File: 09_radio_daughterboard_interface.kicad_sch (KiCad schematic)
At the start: 60 parts, among them J2300 DF40C 60-pin optional radio d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, Q2300 2N7002K radio-PG USB enable, U2300 TPS259470ARPW 2A reverse-bloc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, U2301 TLV803EA43 4.3V radio rail su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, U2302 SN74LVC1G17DBVR radio PG leve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, U2303 TS3USB30E default-disconnecte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, U2304 TPS2553D radio codec VBUS gat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, U2305 USBLC6-2P6 radio codec USB ESD

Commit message: Stamp generation-time BOM catalog; close 378 procurement gaps
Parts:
- C2300: MPN (none) -> GRM155R71H472KA01; Manufacturer (none) -> Murata
- C2301, C2308: MPN (none) -> GRM31CR71E106KA12L; Manufacturer (none) -> Murata
- C2302, C2304, C2305, C2306: MPN (none) -> GRM188R71H104KA93D; Manufacturer (none) -> Murata
- C2303: MPN (none) -> GRM31CZ71C226ME15L; Manufacturer (none) -> Murata
- C2307: MPN (none) -> GRM21BR71E105KA12L; Manufacturer (none) -> Murata
- R2300, R2307: MPN (none) -> RC0603FR-07100KL; Manufacturer (none) -> Yageo
- R2301: MPN (none) -> RT0603BRD071K65L; Manufacturer (none) -> Yageo
- R2302: MPN (none) -> RC0603FR-072K2L; Manufacturer (none) -> Yageo
- R2303, R2305, R2306: MPN (none) -> RC0603FR-0710KL; Manufacturer (none) -> Yageo
- R2304: MPN (none) -> RC0603FR-0720KL; Manufacturer (none) -> Yageo
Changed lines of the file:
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@@
   (property "Footprint" "Resistor_SMD:R_0603_1608Metric" (at 20.32 76.2 0) (effects (font (size 1.27 1.27)) (hide yes)))
   (property "Datasheet" "" (at 20.32 76.2 0) (effects (font (size 1.27 1.27)) (hide yes)))
+  (property "Manufacturer" "Yageo" (at 20.32 76.2 0) (effects (font (size 1.27 1.27)) (hide yes)))
+  (property "MPN" "RC0603FR-07100KL" (at 20.32 76.2 0) (effects (font (size 1.27 1.27)) (hide yes)))
   (pin "1")
   (pin "2")
@@
   (property "Footprint" "Resistor_SMD:R_0603_1608Metric" (at 20.32 88.9 0) (effects (font (size 1.27 1.27)) (hide yes)))
   (property "Datasheet" "" (at 20.32 88.9 0) (effects (font (size 1.27 1.27)) (hide yes)))
+  (property "Manufacturer" "Yageo" (at 20.32 88.9 0) (effects (font (size 1.27 1.27)) (hide yes)))
+  (property "MPN" "RT0603BRD071K65L" (at 20.32 88.9 0) (effects (font (size 1.27 1.27)) (hide yes)))
   (pin "1")
   (pin "2")
@@
   (property "Footprint" "Capacitor_SMD:C_0402_1005Metric" (at 20.32 101.6 0) (effects (font (size 1.27 1.27)) (hide yes)))
   (property "Datasheet" "" (at 20.32 101.6 0) (effects (font (size 1.27 1.27)) (hide yes)))
+  (property "Manufacturer" "Murata" (at 20.32 101.6 0) (effects (font (size 1.27 1.27)) (hide yes)))
+  (property "MPN" "GRM155R71H472KA01" (at 20.32 101.6 0) (effects (font (size 1.27 1.27)) (hide yes)))
   (pin "1")
   (pin "2")
@@
   (property "Footprint" "Capacitor_SMD:C_1206_3216Metric" (at 20.32 114.3 0) (effects (font (size 1.27 1.27)) (hide yes)))
   (property "Datasheet" "" (at 20.32 114.3 0) (effects (font (size 1.27 1.27)) (hide yes)))
+  (property "Manufacturer" "Murata" (at 20.32 114.3 0) (effects (font (size 1.27 1.27)) (hide yes)))
+  (property "MPN" "GRM31CR71E106KA12L" (at 20.32 114.3 0) (effects (font (size 1.27 1.27)) (hide yes)))
   (pin "1")
   (pin "2")
@@
   (property "Footprint" "Capacitor_SMD:C_0603_1608Metric" (at 20.32 127 0) (effects (font (size 1.27 1.27)) (hide yes)))
   (property "Datasheet" "" (at 20.32 127 0) (effects (font (size 1.27 1.27)) (hide yes)))
+  (property "Manufacturer" "Murata" (at 20.32 127 0) (effects (font (size 1.27 1.27)) (hide yes)))
+  (property "MPN" "GRM188R71H104KA93D" (at 20.32 127 0) (effects (font (size 1.27 1.27)) (hide yes)))
   (pin "1")
   (pin "2")
@@
   (property "Footprint" "Capacitor_SMD:C_1206_3216Metric" (at 20.32 139.7 0) (effects (font (size 1.27 1.27)) (hide yes)))
   (property "Datasheet" "" (at 20.32 139.7 0) (effects (font (size 1.27 1.27)) (hide yes)))
+  (property "Manufacturer" "Murata" (at 20.32 139.7 0) (effects (font (size 1.27 1.27)) (hide yes)))
+  (property "MPN" "GRM31CZ71C226ME15L" (at 20.32 139.7 0) (effects (font (size 1.27 1.27)) (hide yes)))
   (pin "1")
   (pin "2")
@@
   (property "Footprint" "Capacitor_SMD:C_0603_1608Metric" (at 20.32 152.4 0) (effects (font (size 1.27 1.27)) (hide yes)))
   (property "Datasheet" "" (at 20.32 152.4 0) (effects (font (size 1.27 1.27)) (hide yes)))
+  (property "Manufacturer" "Murata" (at 20.32 152.4 0) (effects (font (size 1.27 1.27)) (hide yes)))
+  (property "MPN" "GRM188R71H104KA93D" (at 20.32 152.4 0) (effects (font (size 1.27 1.27)) (hide yes)))
   (pin "1")
   (pin "2")
@@
   (property "Footprint" "Resistor_SMD:R_0603_1608Metric" (at 224.79 115.57 0) (effects (font (size 1.27 1.27)) (hide yes)))
   (property "Datasheet" "" (at 224.79 115.57 0) (effects (font (size 1.27 1.27)) (hide yes)))
+  (property "Manufacturer" "Yageo" (at 224.79 115.57 0) (effects (font (size 1.27 1.27)) (hide yes)))
+  (property "MPN" "RC0603FR-072K2L" (at 224.79 115.57 0) (effects (font (size 1.27 1.27)) (hide yes)))
   (pin "1")
   (pin "2")
@@
   (property "Footprint" "Resistor_SMD:R_0603_1608Metric" (at 260.35 115.57 0) (effects (font (size 1.27 1.27)) (hide yes)))
   (property "Datasheet" "" (at 260.35 115.57 0) (effects (font (size 1.27 1.27)) (hide yes)))
+  (property "Manufacturer" "Yageo" (at 260.35 115.57 0) (effects (font (size 1.27 1.27)) (hide yes)))
+  (property "MPN" "RC0603FR-0710KL" (at 260.35 115.57 0) (effects (font (size 1.27 1.27)) (hide yes)))
   (pin "1")
   (pin "2")
@@
   (property "Footprint" "Resistor_SMD:R_0603_1608Metric" (at 299.72 115.57 0) (effects (font (size 1.27 1.27)) (hide yes)))
   (property "Datasheet" "" (at 299.72 115.57 0) (effects (font (size 1.27 1.27)) (hide yes)))
+  (property "Manufacturer" "Yageo" (at 299.72 115.57 0) (effects (font (size 1.27 1.27)) (hide yes)))
+  (property "MPN" "RC0603FR-0720KL" (at 299.72 115.57 0) (effects (font (size 1.27 1.27)) (hide yes)))
   (pin "1")
   (pin "2")
@@
   (property "Footprint" "Capacitor_SMD:C_0603_1608Metric" (at 350.52 124.46 0) (effects (font (size 1.27 1.27)) (hide yes)))
   (property "Datasheet" "" (at 350.52 124.46 0) (effects (font (size 1.27 1.27)) (hide yes)))
+  (property "Manufacturer" "Murata" (at 350.52 124.46 0) (effects (font (size 1.27 1.27)) (hide yes)))
+  (property "MPN" "GRM188R71H104KA93D" (at 350.52 124.46 0) (effects (font (size 1.27 1.27)) (hide yes)))
   (pin "1")
   (pin "2")
@@
   (property "Footprint" "Resistor_SMD:R_0603_1608Metric" (at 420.37 76.2 0) (effects (font (size 1.27 1.27)) (hide yes)))
   (property "Datasheet" "" (at 420.37 76.2 0) (effects (font (size 1.27 1.27)) (hide yes)))
+  (property "Manufacturer" "Yageo" (at 420.37 76.2 0) (effects (font (size 1.27 1.27)) (hide yes)))
+  (property "MPN" "RC0603FR-0710KL" (at 420.37 76.2 0) (effects (font (size 1.27 1.27)) (hide yes)))
   (pin "1")
   (pin "2")
@@
   (property "Footprint" "Resistor_SMD:R_0603_1608Metric" (at 420.37 88.9 0) (effects (font (size 1.27 1.27)) (hide yes)))
   (property "Datasheet" "" (at 420.37 88.9 0) (effects (font (size 1.27 1.27)) (hide yes)))
+  (property "Manufacturer" "Yageo" (at 420.37 88.9 0) (effects (font (size 1.27 1.27)) (hide yes)))
+  (property "MPN" "RC0603FR-0710KL" (at 420.37 88.9 0) (effects (font (size 1.27 1.27)) (hide yes)))
   (pin "1")
   (pin "2")
@@
   (property "Footprint" "Resistor_SMD:R_0603_1608Metric" (at 20.32 228.6 0) (effects (font (size 1.27 1.27)) (hide yes)))
   (property "Datasheet" "" (at 20.32 228.6 0) (effects (font (size 1.27 1.27)) (hide yes)))
+  (property "Manufacturer" "Yageo" (at 20.32 228.6 0) (effects (font (size 1.27 1.27)) (hide yes)))
+  (property "MPN" "RC0603FR-07100KL" (at 20.32 228.6 0) (effects (font (size 1.27 1.27)) (hide yes)))
   (pin "1")
   (pin "2")
@@
   (property "Footprint" "Capacitor_SMD:C_0603_1608Metric" (at 20.32 254 0) (effects (font (size 1.27 1.27)) (hide yes)))
   (property "Datasheet" "" (at 20.32 254 0) (effects (font (size 1.27 1.27)) (hide yes)))
+  (property "Manufacturer" "Murata" (at 20.32 254 0) (effects (font (size 1.27 1.27)) (hide yes)))
+  (property "MPN" "GRM188R71H104KA93D" (at 20.32 254 0) (effects (font (size 1.27 1.27)) (hide yes)))
   (pin "1")
   (pin "2")
@@
   (property "Footprint" "Capacitor_SMD:C_0805_2012Metric" (at 430.53 241.3 0) (effects (font (size 1.27 1.27)) (hide yes)))
   (property "Datasheet" "" (at 430.53 241.3 0) (effects (font (size 1.27 1.27)) (hide yes)))
+  (property "Manufacturer" "Murata" (at 430.53 241.3 0) (effects (font (size 1.27 1.27)) (hide yes)))
+  (property "MPN" "GRM21BR71E105KA12L" (at 430.53 241.3 0) (effects (font (size 1.27 1.27)) (hide yes)))
   (pin "1")
   (pin "2")
@@
   (property "Footprint" "Capacitor_SMD:C_1206_3216Metric" (at 430.53 254 0) (effects (font (size 1.27 1.27)) (hide yes)))
   (property "Datasheet" "" (at 430.53 254 0) (effects (font (size 1.27 1.27)) (hide yes)))
-  (pin "1")
-  (pin "2")
+  (property "Manufacturer" "Murata" (at 430.53 254 0) (effects (font (size 1.27 1.27)) (hide yes)))
+  (property "MPN" "GRM31CR71E106KA12L" (at 430.53 254 0) (effects (font (size 1.27 1.27)) (hide yes)))
+  (pin "1")
+  (pin "2")

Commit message: Swap radio daughterboard connector: DF40-60 -> FH12-30S FFC
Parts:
- J2300: value DF40C 60-pin optional radio daughterboard plug -> FH12-30S 30-pin radio daughterboard FFC; footprint Connector_Hirose_DF40:Hirose_DF40C-60DP-0.4V_2x30-1MP_P0.4mm -> Connector_FFC-FPC:Hirose_FH12-30S-0.5SH_1x30-1MP_P0.50mm_Horizontal; symbol Conn_02x30_MP:Conn_02x30_MP -> Conn_01x30_FFC_MP:Conn_01x30_FFC_MP
- R2340: value 4.7k J2300 pin 23 signal isolation -> 4.7k J2300 pin 11 signal isolation
- R2341: value 4.7k J2300 pin 24 signal isolation -> 4.7k J2300 pin 12 signal isolation
- R2342: value 4.7k J2300 pin 25 signal isolation -> 4.7k J2300 pin 13 signal isolation
- R2343: value 4.7k J2300 pin 26 signal isolation -> 4.7k J2300 pin 14 signal isolation
- R2344: value 4.7k J2300 pin 28 signal isolation -> 4.7k J2300 pin 15 signal isolation
- R2345: value 4.7k J2300 pin 29 signal isolation -> 4.7k J2300 pin 16 signal isolation
- R2346: value 4.7k J2300 pin 30 signal isolation -> 4.7k J2300 pin 17 signal isolation
- R2347: value 4.7k J2300 pin 31 signal isolation -> 4.7k J2300 pin 18 signal isolation
- R2348: value 4.7k J2300 pin 33 signal isolation -> 4.7k J2300 pin 20 signal isolation
- R2349: value 4.7k J2300 pin 34 signal isolation -> 4.7k J2300 pin 21 signal isolation
- R2350: value 4.7k J2300 pin 35 signal isolation -> 4.7k J2300 pin 22 signal isolation
- R2351: value 4.7k J2300 pin 36 signal isolation -> 4.7k J2300 pin 23 signal isolation
- R2352: value 4.7k J2300 pin 38 signal isolation -> 4.7k J2300 pin 24 signal isolation
- R2353: value 4.7k J2300 pin 39 signal isolation -> 4.7k J2300 pin 25 signal isolation
- R2354: value 4.7k J2300 pin 40 signal isolation -> 4.7k J2300 pin 27 signal isolation
- R2355: value 4.7k J2300 pin 41 signal isolation -> 4.7k J2300 pin 28 signal isolation
- R2356: value 4.7k J2300 pin 42 signal isolation -> 4.7k J2300 pin 29 signal isolation
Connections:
- net GND: now also J2300.1 (Pin_1), J2300.19 (Pin_19), J2300.26 (Pin_26), J2300.4 (Pin_4), J2300.7 (Pin_7); no longer J2300.11 (Pin_11), J2300.12 (Pin_12), J2300.13 (Pin_13), J2300.14 (Pin_14), J2300.15 (Pin_15), J2300.16 (Pin_16), J2300.21 (Pin_21), J2300.22 (Pin_22), J2300.27 (Pin_27), J2300.32 (Pin_32), J2300.37 (Pin_37), J2300.43 (Pin_43), J2300.45 (Pin_45), J2300.46 (Pin_46), J2300.47 (Pin_47), J2300.48 (Pin_48), J2300.49 (Pin_49), J2300.50 (Pin_50), J2300.51 (Pin_51), J2300.52 (Pin_52), J2300.53 (Pin_53), J2300.54 (Pin_54), J2300.55 (Pin_55), J2300.56 (Pin_56), J2300.57 (Pin_57), J2300.58 (Pin_58), J2300.59 (Pin_59), J2300.60 (Pin_60), J2300.9 (Pin_9)
- net GNSS_EXTINT_DB: now also J2300.29 (Pin_29); no longer J2300.42 (Pin_42)
- net GNSS_PPS_DB: now also J2300.28 (Pin_28); no longer J2300.41 (Pin_41)
- net GNSS_RESET_N_DB: now also J2300.27 (Pin_27); no longer J2300.40 (Pin_40)
- net GNSS_UART_RX_DB: now also J2300.24 (Pin_24); no longer J2300.38 (Pin_38)
- net GNSS_UART_TX_DB: now also J2300.25 (Pin_25); no longer J2300.39 (Pin_39)
- net RADIO_CODEC_USB_DM_DB: now also J2300.9 (Pin_9); no longer J2300.20 (Pin_20)
- net RADIO_CODEC_USB_DP_DB: now also J2300.8 (Pin_8); no longer J2300.19 (Pin_19)
- net RADIO_CODEC_USB_VBUS_DB: now also J2300.5 (Pin_5); no longer J2300.17 (Pin_17), J2300.18 (Pin_18)
- net RADIO_DB_5V: no longer J2300.1 (Pin_1), J2300.4 (Pin_4), J2300.5 (Pin_5), J2300.7 (Pin_7), J2300.8 (Pin_8)
- net RADIO_DB_PRESENT_N: now also J2300.30 (Pin_30); no longer J2300.44 (Pin_44)
- net RADIO_UHF_PD_N_DB: now also J2300.18 (Pin_18); no longer J2300.31 (Pin_31)
- net RADIO_UHF_PTT_N_DB: now also J2300.16 (Pin_16); no longer J2300.29 (Pin_29)
- net RADIO_UHF_RF_SEL_3V3_DB: now also J2300.23 (Pin_23); no longer J2300.36 (Pin_36)
- net RADIO_UHF_SQL_DB: now also J2300.21 (Pin_21); no longer J2300.34 (Pin_34)
- net RADIO_UHF_UART_RX_DB: now also J2300.14 (Pin_14); no longer J2300.26 (Pin_26)
- net RADIO_UHF_UART_TX_DB: now also J2300.13 (Pin_13); no longer J2300.25 (Pin_25)
- net RADIO_VHF_PD_N_DB: now also J2300.17 (Pin_17); no longer J2300.30 (Pin_30)
- net RADIO_VHF_PTT_N_DB: now also J2300.15 (Pin_15); no longer J2300.28 (Pin_28)
- net RADIO_VHF_RF_SEL_3V3_DB: now also J2300.22 (Pin_22); no longer J2300.35 (Pin_35)
- net RADIO_VHF_SQL_DB: now also J2300.20 (Pin_20); no longer J2300.33 (Pin_33)
- net RADIO_VHF_UART_RX_DB: now also J2300.12 (Pin_12); no longer J2300.24 (Pin_24)
- net RADIO_VHF_UART_TX_DB: now also J2300.11 (Pin_11); no longer J2300.23 (Pin_23)
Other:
- note added: "FH12-30S 30-pin FFC: three 5V pins, interleaved GND for return/shielding; route them as short, wide pours with stitching vias."
- note added: "J2300 pin 30 is passively grounded on the daughterboard. High means absent; low means physically installed."
- note added: "R2340-R2352 limit fault current on every GPIO/UART/control line crossing the FFC."
- note removed: "Eight DF40 contacts share RADIO_DB_5V and thirty contacts are ground; route them as short, wide pours with stitching vias."
- note removed: "J2300 pin 44 is passively grounded only on the daughterboard. High means absent; low means physically installed."
- note removed: "R2340-R2356 limit fault current on every removable-board GPIO/UART/control line; no signal pin directly crosses J2300."

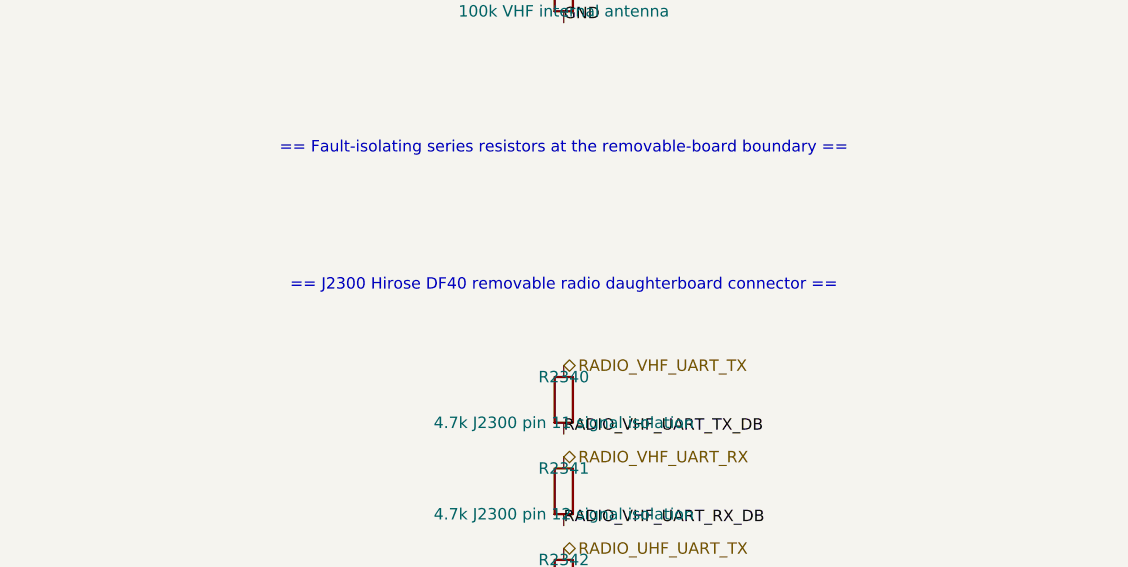
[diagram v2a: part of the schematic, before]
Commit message: F4: J2300 fully on-board, fix FH12-30S BOM properties
J2300 (FH12-30S FFC at the radio DB edge) had all 30 signal pads
reaching y=185.5 - off the 185mm board bottom edge (2 copper_edge
violations, connector body overhanging). Moved north to (62.5, 181):
pads now max at y=183.5. Moved C725 clear of the MP pad.

Fixed the BOM trap: PCB J2300 properties still said MPN
DF40C-60DP-0.4V(51) / MatingConnector DF40C(2.0)-60DS-0.4V(51) (the
old 60-pin part - a BOM run would order the wrong connector).
Updated to FH12-30S-0.5SH(55) / FH12 30-pin 0.5mm FFC cable in both
the schematic generator and the PCB.

DRC: 841 -> 840, copper_edge_clearance 2 -> 0, 0 shorts.
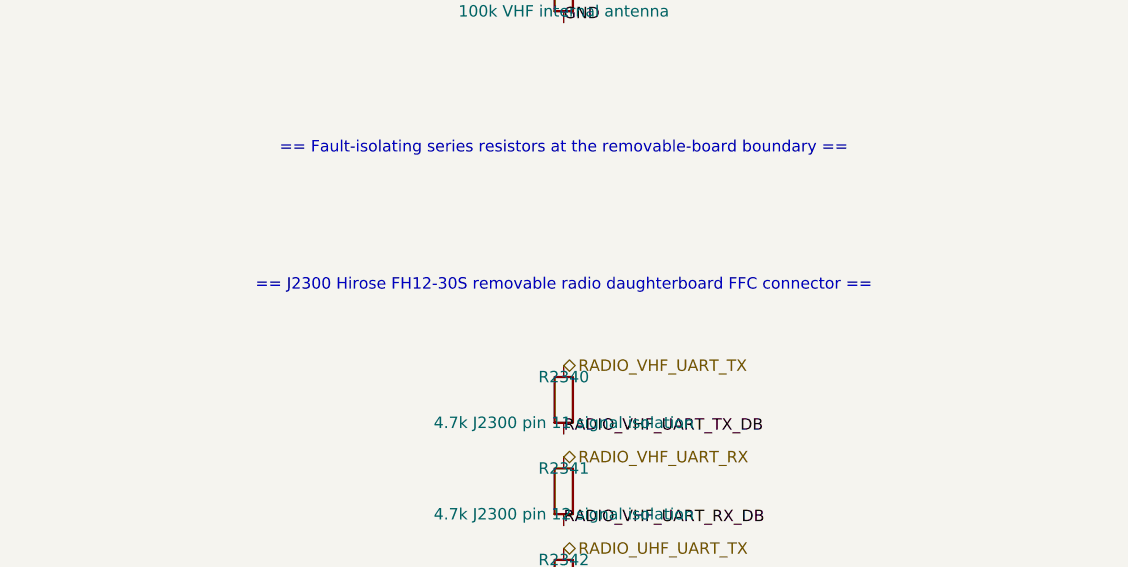
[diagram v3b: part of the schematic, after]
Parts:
- J2300: MPN DF40C-60DP-0.4V(51) -> FH12-30S-0.5SH(55); MatingConnector DF40C(2.0)-60DS-0.4V(51) -> FH12 series 30-pin 0.5mm-pitch FFC cable
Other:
- note added: "== J2300 Hirose FH12-30S removable radio daughterboard FFC connector =="
- note removed: "== J2300 Hirose DF40 removable radio daughterboard connector =="
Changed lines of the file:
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@@
   (effects (font (size 1.27 1.27)) (justify left bottom))
 )
-(text "== J2300 Hirose DF40 removable radio daughterboard connector ==" (at 20.32 414.02 0) (effects (font (size 1.27 1.27))))
+(text "== J2300 Hirose FH12-30S removable radio daughterboard FFC connector ==" (at 20.32 414.02 0) (effects (font (size 1.27 1.27))))
 (symbol
   (lib_id "Conn_01x30_FFC_MP:Conn_01x30_FFC_MP")
@@
   (property "Datasheet" "" (at 369.57 539.75 0) (effects (font (size 1.27 1.27)) (hide yes)))
   (property "Manufacturer" "Hirose Electric" (at 369.57 539.75 0) (effects (font (size 1.27 1.27)) (hide yes)))
-  (property "MPN" "DF40C-60DP-0.4V(51)" (at 369.57 539.75 0) (effects (font (size 1.27 1.27)) (hide yes)))
-  (property "MatingConnector" "DF40C(2.0)-60DS-0.4V(51)" (at 369.57 539.75 0) (effects (font (size 1.27 1.27)) (hide yes)))
+  (property "MPN" "FH12-30S-0.5SH(55)" (at 369.57 539.75 0) (effects (font (size 1.27 1.27)) (hide yes)))
+  (property "MatingConnector" "FH12 series 30-pin 0.5mm-pitch FFC cable" (at 369.57 539.75 0) (effects (font (size 1.27 1.27)) (hide yes)))
   (property "StackHeight" "2.0mm" (at 369.57 539.75 0) (effects (font (size 1.27 1.27)) (hide yes)))
   (property "AbsentBoardContract" "NO_RADIO_BOARD_REQUIRED_FOR_BOOT_OR_PRIMARY_LAPTOP_OPERATION" (at 369.57 539.75 0) (effects (font (size 1.27 1.27)) (hide yes)))
